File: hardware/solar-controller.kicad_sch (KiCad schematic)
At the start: 0 parts

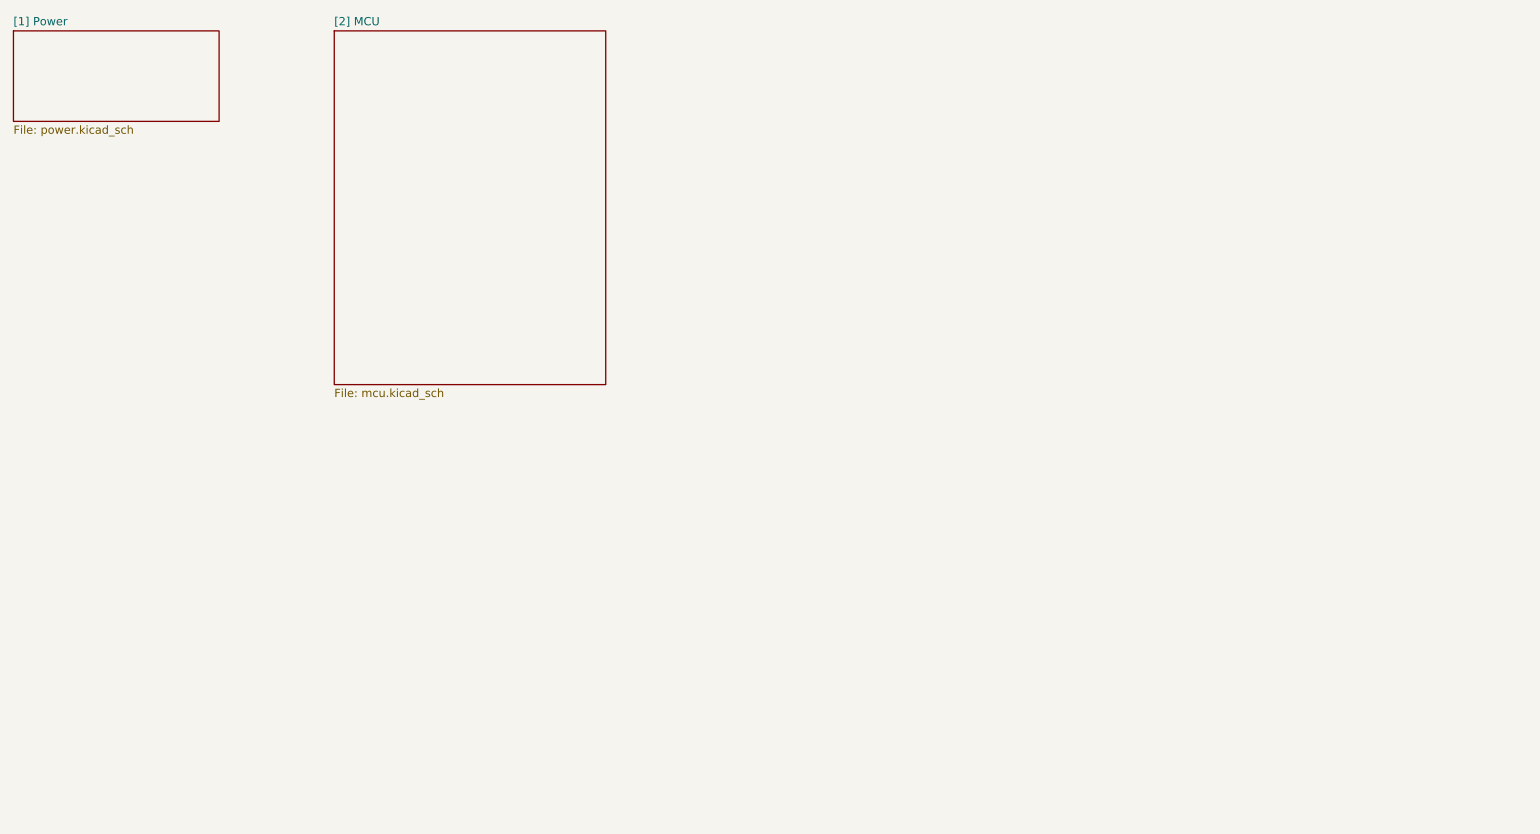
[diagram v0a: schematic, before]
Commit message: feat: Added led controller sheet
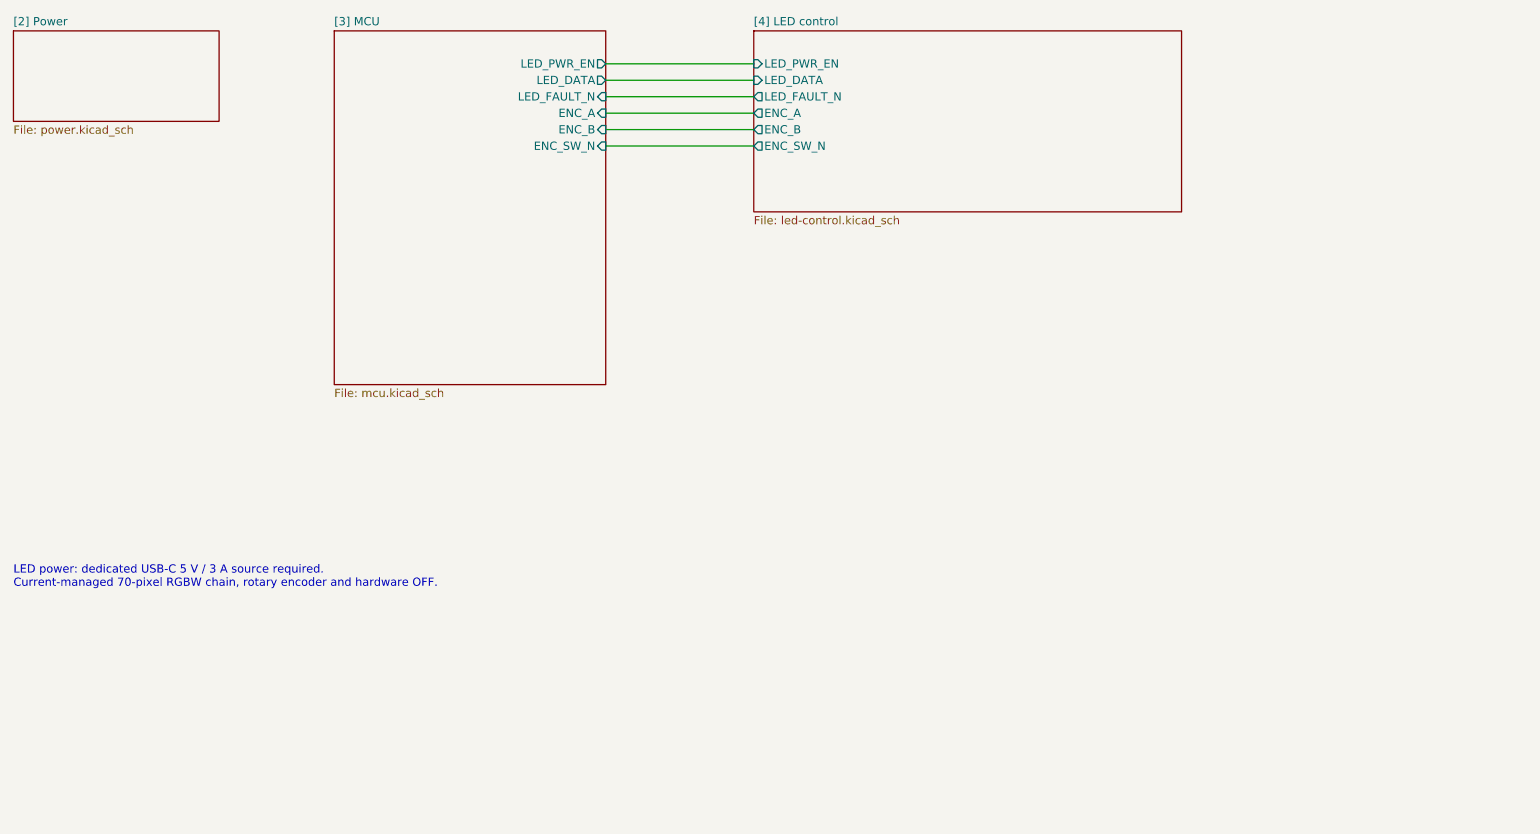
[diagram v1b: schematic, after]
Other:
- sheet [1] Power renamed [2] Power
- sheet [2] MCU renamed [3] MCU
- added sheet [4] LED control (led-control.kicad_sch)
- sheet [3] MCU ports: added ENC_A, ENC_B, ENC_SW_N, LED_DATA, LED_FAULT_N, LED_PWR_EN; removed none
- note added: "LED power: dedicated USB-C 5 V / 3 A source required. Current-managed 70-pixel RGBW chain, rotary encoder and hardware OFF."
- title: (none) -> LED power and controls
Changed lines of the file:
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@@
 	(paper "A4")
 	(title_block
+		(title "LED power and controls")
 		(rev "1")
-		(comment 1 "Design for JLCPCB Service")
+		(comment 1 "JLCPCB")
+	)
+	(text "LED power: dedicated USB-C 5 V / 3 A source required.\nCurrent-managed 70-pixel RGBW chain, rotary encoder and hardware OFF."
+		(exclude_from_sim no)
+		(at 48.26 124.46 0)
+		(effects
+			(font
+				(size 1.27 1.27)
+			)
+			(justify left top)
+		)
+	)
+	(wire
+		(pts
+			(xy 139.7 59.69) (xy 162.56 59.69)
+		)
+		(stroke
+			(width 0)
+			(type default)
+		)
+	)
+	(wire
+		(pts
+			(xy 139.7 46.99) (xy 162.56 46.99)
+		)
+		(stroke
+			(width 0)
+			(type default)
+		)
+	)
+	(wire
+		(pts
+			(xy 139.7 49.53) (xy 162.56 49.53)
+		)
+		(stroke
+			(width 0)
+			(type default)
+		)
+	)
+	(wire
+		(pts
+			(xy 139.7 54.61) (xy 162.56 54.61)
+		)
+		(stroke
+			(width 0)
+			(type default)
+		)
+	)
+	(wire
+		(pts
+			(xy 139.7 57.15) (xy 162.56 57.15)
+		)
+		(stroke
+			(width 0)
+			(type default)
+		)
+	)
+	(wire
+		(pts
+			(xy 139.7 52.07) (xy 162.56 52.07)
+		)
+		(stroke
+			(width 0)
+			(type default)
+		)
 	)
 	(sheet
@@
 			(color 0 0 0 0)
 		)
-		(property "Sheetname" "[1] Power"
+		(property "Sheetname" "[2] Power"
 			(at 48.26 41.1984 0)
 			(show_name no)
@@
 			(color 0 0 0 0)
 		)
-		(property "Sheetname" "[2] MCU"
+		(property "Sheetname" "[3] MCU"
 			(at 97.79 41.1984 0)
 			(show_name no)
@@
 				)
 				(justify left top)
+			)
+		)
+		(pin "LED_PWR_EN" output
+			(at 139.7 46.99 0)
+			(effects
+				(font
+					(size 1.27 1.27)
+				)
+				(justify right)
+			)
+		)
+		(pin "LED_DATA" output
+			(at 139.7 49.53 0)
+			(effects
+				(font
+					(size 1.27 1.27)
+				)
+				(justify right)
+			)
+		)
+		(pin "LED_FAULT_N" input
+			(at 139.7 52.07 0)
+			(effects
+				(font
+					(size 1.27 1.27)
+				)
+				(justify right)
+			)
+		)
+		(pin "ENC_A" input
+			(at 139.7 54.61 0)
+			(effects
+				(font
+					(size 1.27 1.27)
+				)
+				(justify right)
+			)
+		)
+		(pin "ENC_B" input
+			(at 139.7 57.15 0)
+			(effects
+				(font
+					(size 1.27 1.27)
+				)
+				(justify right)
+			)
+		)
+		(pin "ENC_SW_N" input
+			(at 139.7 59.69 0)
+			(effects
+				(font
+					(size 1.27 1.27)
+				)
+				(justify right)
 			)
 		)
@@
 				)
 			)
+		)
+	)
+	(sheet
+		(at 162.56 41.91)
+		(size 66.04 27.94)
+		(exclude_from_sim no)
+		(in_bom yes)
+		(on_board yes)
+		(dnp no)
+		(fields_autoplaced yes)
+		(stroke
+			(width 0.1524)
+			(type solid)
+		)
+		(fill
+			(color 0 0 0 0)
+		)
+		(property "Sheetname" "[4] LED control"
+			(at 162.56 41.1984 0)
+			(show_name no)
+			(do_not_autoplace no)
+			(effects
+				(font
+					(size 1.27 1.27)
+				)
+				(justify left bottom)
+			)
+		)
+		(property "Sheetfile" "led-control.kicad_sch"
+			(at 162.56 70.4346 0)
+			(show_name no)
+			(do_not_autoplace no)
+			(effects
+				(font
+					(size 1.27 1.27)
+				)
+				(justify left top)
+			)
+		)
+		(pin "LED_PWR_EN" input
+			(at 162.56 46.99 180)
+			(effects
+				(font
+					(size 1.27 1.27)
+				)
+				(justify left)
+			)
+		)
+		(pin "LED_DATA" input
+			(at 162.56 49.53 180)
+			(effects
+				(font
+					(size 1.27 1.27)
+				)
+				(justify left)
+			)
+		)
+		(pin "LED_FAULT_N" output
+			(at 162.56 52.07 180)
+			(effects
+				(font
+					(size 1.27 1.27)
+				)
+				(justify left)
+			)
+		)
+		(pin "ENC_A" output
+			(at 162.56 54.61 180)
+			(effects
+				(font
+					(size 1.27 1.27)
+				)
+				(justify left)
+			)
+		)
+		(pin "ENC_B" output
+			(at 162.56 57.15 180)
+			(effects
+				(font
+					(size 1.27 1.27)
+				)
+				(justify left)
+			)
+		)
+		(pin "ENC_SW_N" output
+			(at 162.56 59.69 180)
+			(effects
+				(font
+					(size 1.27 1.27)
+				)
+				(justify left)
+			)
+		)
+		(instances
+			(project "solar-controller"
+				(path "/1ebd2a79-85df-49b0-bc4d-96f69f4cf347"
+					(page "4")
+				)
+			)

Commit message: feat: WIP pcb layout
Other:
- sheet [3] MCU ports: added LED_ISENSE, MCU_LDATA; removed LED_DATA
- sheet [4] LED control ports: added LED_ISENSE, MCU_LDATA; removed LED_DATA
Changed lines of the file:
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@@
+	(wire
+		(pts
+			(xy 139.7 62.23) (xy 162.56 62.23)
+		)
+		(stroke
+			(width 0)
+			(type default)
+		)
+	)
 	(wire
 		(pts
@@
 			)
 		)
-		(pin "LED_DATA" output
-			(at 139.7 49.53 0)
-			(effects
-				(font
-					(size 1.27 1.27)
-				)
-				(justify right)
-			)
-		)
 		(pin "LED_FAULT_N" input
 			(at 139.7 52.07 0)
@@
 		(pin "ENC_SW_N" input
 			(at 139.7 59.69 0)
+			(effects
+				(font
+					(size 1.27 1.27)
+				)
+				(justify right)
+			)
+		)
+		(pin "LED_ISENSE" input
+			(at 139.7 62.23 0)
+			(effects
+				(font
+					(size 1.27 1.27)
+				)
+				(justify right)
+			)
+		)
+		(pin "MCU_LDATA" output
+			(at 139.7 49.53 0)
 			(effects
 				(font
@@
 			)
 		)
-		(pin "LED_DATA" input
-			(at 162.56 49.53 180)
-			(effects
-				(font
-					(size 1.27 1.27)
-				)
-				(justify left)
-			)
-		)
 		(pin "LED_FAULT_N" output
 			(at 162.56 52.07 180)
@@
 			(effects
 				(font
+					(size 1.27 1.27)
+				)
+				(justify left)
+			)
+		)
+		(pin "LED_ISENSE" output
+			(at 162.56 62.23 180)
+			(effects
+				(font
+					(size 1.27 1.27)
+				)
+				(justify left)
+			)
+		)
+		(pin "MCU_LDATA" input
+			(at 162.56 49.53 180)
+			(effects
+				(font

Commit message: Updated silkscreen and production files
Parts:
- added H101, H102, H103, H104: GND, MountingHole:MountingHole_2.7mm_M2.5_ISO14580_Pad, symbol Mechanical:MountingHole_Pad
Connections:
- new net GND: H101.1, H102.1, H103.1, H104.1
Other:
- note added: "Mounting Holes (M2.5)"
